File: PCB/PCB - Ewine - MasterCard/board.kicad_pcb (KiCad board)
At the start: 2 copper layers, 40.4 x 42 mm, 47 parts, among them J1 FH12-10S-0.5SH_55_, J10 DebugConnector, J2 527450697, J3 FH12-10S-0.5SH_55_, J4 1660, J5 Conn_02x04_Counter_Clockwise, J6 Conn_02x04_Counter_Clockwise, J7 Conn_02x04_Counter_Clockwise, J8 Conn_02x03_Counter_Clockwise, J9 Conn_02x04_Counter_Clockwise, SW1 reset_btn, U3 STM32WB55RGV7, Y1 CM8V-T1A-0.3-32.768KHZ-12.5PF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

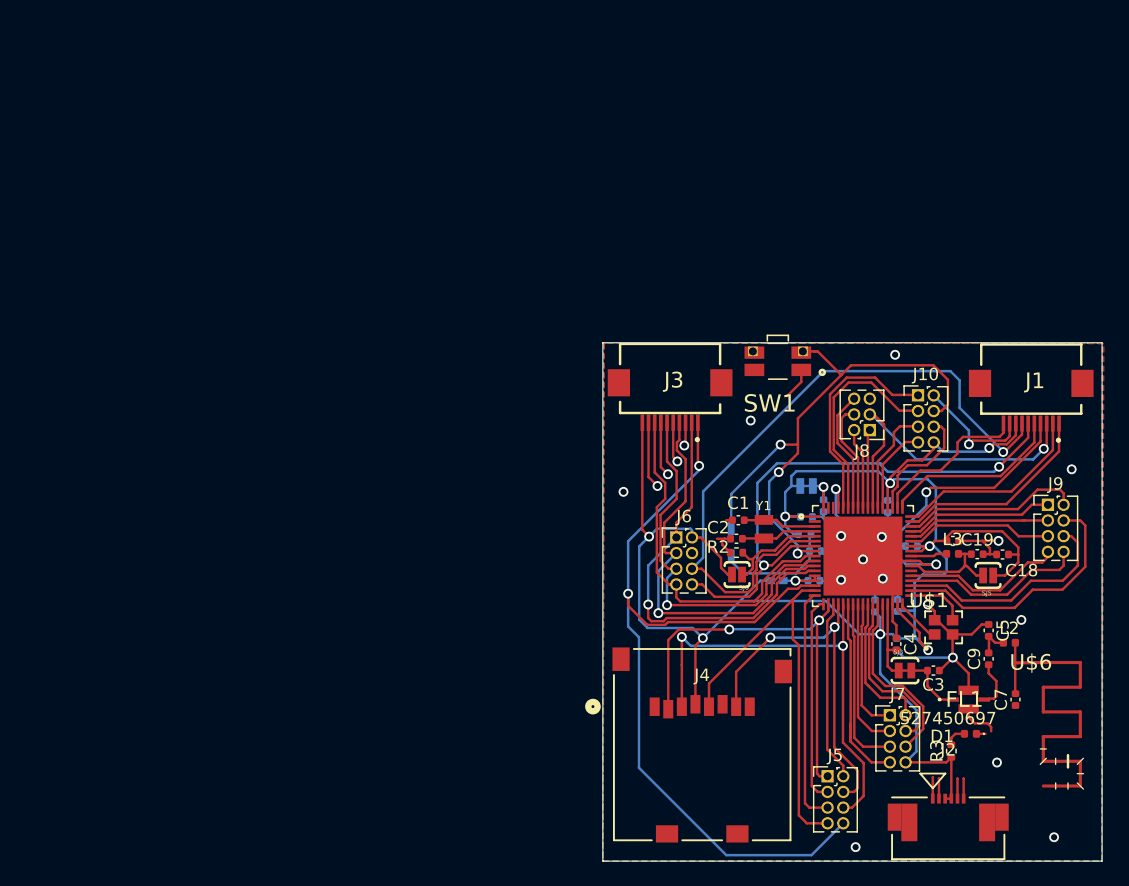
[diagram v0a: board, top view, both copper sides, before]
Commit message: pcb master card ok + il reste à mettre les pins des capteurs restants
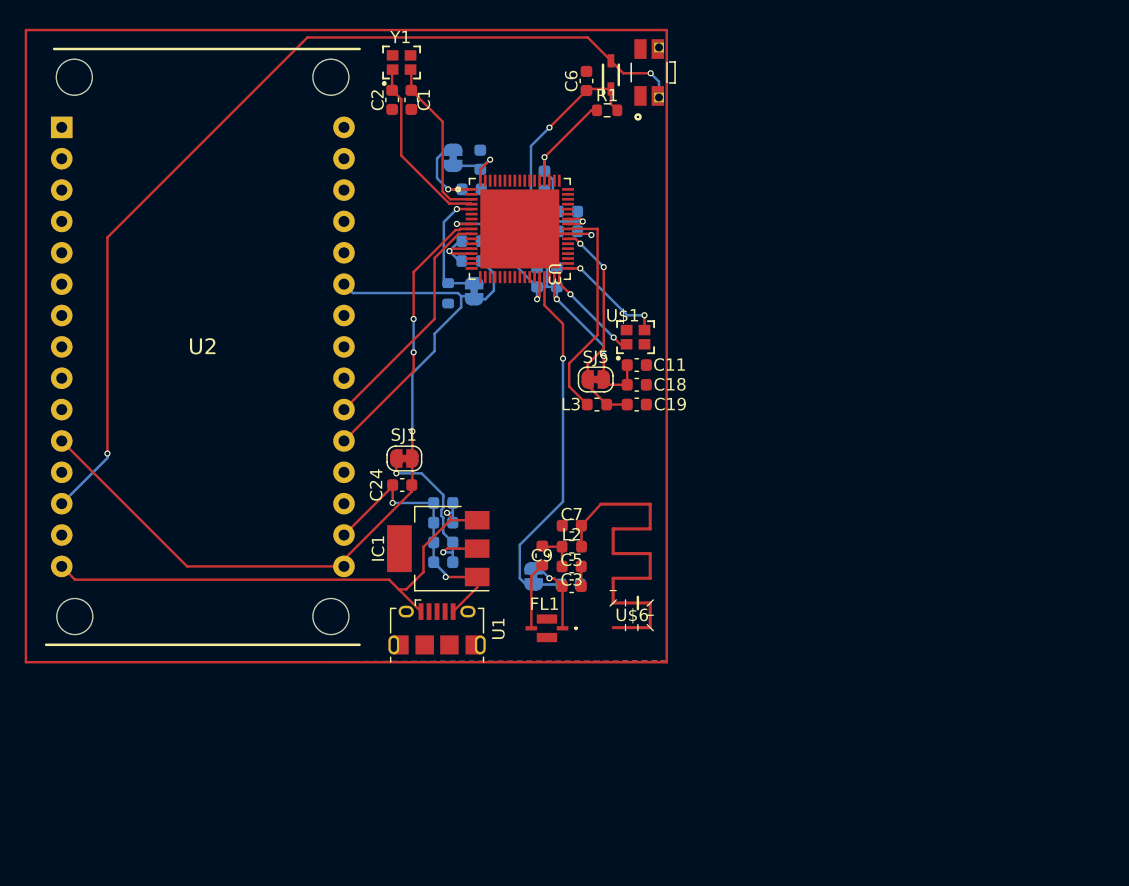
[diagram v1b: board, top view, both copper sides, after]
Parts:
- removed D1: LED, LED_SMD:LED_0402_1005Metric
- removed J1, J3: FH12-10S-0.5SH_55_, FH12-10S-0.5SH_55:FH12-10S-0.5SH(55)
- removed J10: DebugConnector, Connector_PinHeader_1.27mm:PinHeader_2x04_P1.27mm_Vertical
- removed J2: 527450697, ConnectorFPC0.5-6C:CON_527450697_MOL
- removed J4: 1660, CarteSD:CONN_1660_ADA
- removed J5, J6, J7, J9: Conn_02x04_Counter_Clockwise, Connector_PinHeader_1.27mm:PinHeader_2x04_P1.27mm_Vertical
- removed J8: Conn_02x03_Counter_Clockwise, Connector_PinHeader_1.27mm:PinHeader_2x03_P1.27mm_Vertical
- removed R3: 500, Resistor_SMD:R_0402_1005Metric
- added C20: 1µF, Capacitor_SMD:C_0603_1608Metric, B.Cu at (204.2, 74.0)
- added C21: 100nF, Capacitor_SMD:C_0603_1608Metric, B.Cu at (204.2, 75.6)
- added C22: 100nF, Capacitor_SMD:C_0603_1608Metric, B.Cu at (204.2, 77.2)
- added C23: 1µF, Capacitor_SMD:C_0603_1608Metric, B.Cu at (204.2, 78.8)
- added C24: 4.7µF, Capacitor_SMD:C_0603_1608Metric, F.Cu at (200.9, 72.5)
- added IC1: REG1117, Package_TO_SOT_SMD:SOT-223, F.Cu at (203.8, 77.7)
- added SJ1: JUMPER-PAD-2-NC_BY_TRACENO_SILK, Jumper:SolderJumper-2_P1.3mm_Bridged_RoundedPad1.0x1.5mm, F.Cu at (201.1, 70.4)
- added U1: 473460001, Connector_USB:USB_Micro-B_Amphenol_10118194_Horizontal, F.Cu at (203.7, 84.2)
- added U2: 113990105, footprint:113990105, F.Cu at (173.3, 43.6)
- C1, C10, C11, C12, C13, C14, C15, C16, C17, C18, C19, C2, C3, C5, C7, C8, C9: footprint Capacitor_SMD:C_0402_1005Metric -> Capacitor_SMD:C_0603_1608Metric
- C4: footprint Capacitor_SMD:C_0402_1005Metric -> Capacitor_SMD:C_0603_1608Metric; moved to B.Cu
- C6: footprint Capacitor_SMD:C_0402_1005Metric -> Capacitor_SMD:C_0603_1608Metric; moved to F.Cu
- D2: footprint BAT54:SOD2513X117N -> Library:STM32WB55RG_Diode; moved to F.Cu
- FL1: footprint PassBandFI212B245026-T:FI212B245026T -> Library:STM32WB55RG_PassBand
- L1: footprint board:IND_BLM15_0402_MUR -> Inductor_SMD:L_0603_1608Metric
- L2, L3: footprint Inductor_SMD:L_0402_1005Metric -> Inductor_SMD:L_0603_1608Metric
- R1: footprint Resistor_SMD:R_0402_1005Metric -> Resistor_SMD:R_0603_1608Metric; moved to F.Cu
- R2: footprint Resistor_SMD:R_0402_1005Metric -> Resistor_SMD:R_0603_1608Metric; moved to B.Cu
- SJ3: footprint board:PAD-JUMPER-2-NC_BY_TRACE_YES_SILK -> Jumper:SolderJumper-2_P1.3mm_Bridged_RoundedPad1.0x1.5mm; moved to B.Cu
- SJ4: footprint board:PAD-JUMPER-2-NC_BY_TRACE_NO_SILK -> Jumper:SolderJumper-2_P1.3mm_Bridged_RoundedPad1.0x1.5mm
- SJ5: footprint board:PAD-JUMPER-2-NC_BY_PASTE_YES_SILK -> Jumper:SolderJumper-2_P1.3mm_Bridged_RoundedPad1.0x1.5mm
- SJ6: footprint board:PAD-JUMPER-2-NC_BY_PASTE_YES_SILK -> Jumper:SolderJumper-2_P1.3mm_Bridged_RoundedPad1.0x1.5mm; moved to B.Cu
- SW1: footprint SideBtn434331013822:SW_434331013822 -> Library:STM32WB55RG_ResetButton
- U$1: footprint board:BT-XTAL_2016_N -> Library:STM32WB55RG_XTAL
- U$6: footprint board:QWMP_MEANDERED_LEFT_+6 -> Library:STM32WB55RG_BleAntenna
- U3: footprint STM32WB55RGV7:QFN40P800X800X100-69N -> Library:STM32WB55RG
- Y1: footprint board:XTAL_CM8V-T1A-0.3-32.768KHZ-12.5PF-100PPM-TC-QC -> Library:STM32WB55RG_XTAL
- moved Y1 49.5 mm to (199.8, 37.1), turned to 0 degrees
- moved C2 45.2 mm to (200.1, 41.4), turned to -90 degrees
- moved C14 44.0 mm to (214.3, 50.4), turned to 180 degrees
- moved C1 43.1 mm to (201.6, 41.4), turned to -90 degrees
- moved C6 42.4 mm to (215.8, 39.8), turned to -90 degrees
- moved C15 40.4 mm to (214.3, 52.0), turned to 180 degrees
- moved D2 40.3 mm to (213.8, 39.3)
- moved C13 39.5 mm to (207.2, 46.2), turned to 90 degrees
- moved SJ4 39.1 mm to (205.0, 46.0), turned to 90 degrees
- moved C17 39.1 mm to (206.5, 52.8)
- moved C7 38.6 mm to (214.6, 75.8), turned to 0 degrees
- moved C12 38.3 mm to (212.4, 47.9)
- moved C16 37.9 mm to (206.5, 48.6)
- moved R1 37.9 mm to (217.5, 42.2)
- moved U3 37.5 mm to (211.3, 52.2)
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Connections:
- U3 pad 10: ADC2 -> PC1
- U3 pad 11: ADC3 -> PC2
- U3 pad 12: ADC4 -> PC3
- U3 pad 15: ADC5 -> PA0
- U3 pad 16: CLK -> PA1
- U3 pad 19: CS -> PA4
- U3 pad 21: DO -> PA6
- U3 pad 22: DI -> PA7
- U3 pad 50: INT2 -> PC6
- U3 pad 51: INT1 -> PA10
- U3 pad 53: EN -> PA12
- U3 pad 58: GPIO -> PC10
- U3 pad 65: CS_D -> PB5
- U3 pad 9: ADC1 -> PC0
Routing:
- net ADC5: track 69.3 -> 0.00 mm, vias 2 -> 0
- net GND: track 87.4 -> 30.6 mm, vias 22 -> 3
- net PB8: track 55.5 -> 0.00 mm, vias 1 -> 0
- net PB9: track 45.3 -> 0.00 mm, vias 2 -> 0
- net 5V: track 0.00 -> 43.3 mm, vias 0 -> 1
- net VDD: track 165.6 -> 126.3 mm, vias 8 -> 7
- net DI: track 37.3 -> 0.00 mm, vias 2 -> 0
- net CLK: track 33.8 -> 0.00 mm
- net CS: track 33.5 -> 0.00 mm, vias 2 -> 0
- net ADC4: track 33.4 -> 0.00 mm, vias 1 -> 0
- net ADC3: track 32.8 -> 0.00 mm, vias 1 -> 0
- net NRST: track 45.6 -> 77.3 mm, vias 3 -> 2
- net ADC2: track 30.8 -> 0.00 mm, vias 1 -> 0
- net DO: track 29.4 -> 0.00 mm, vias 2 -> 0
- net ADC1: track 29.2 -> 0.00 mm
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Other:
- board outline removed

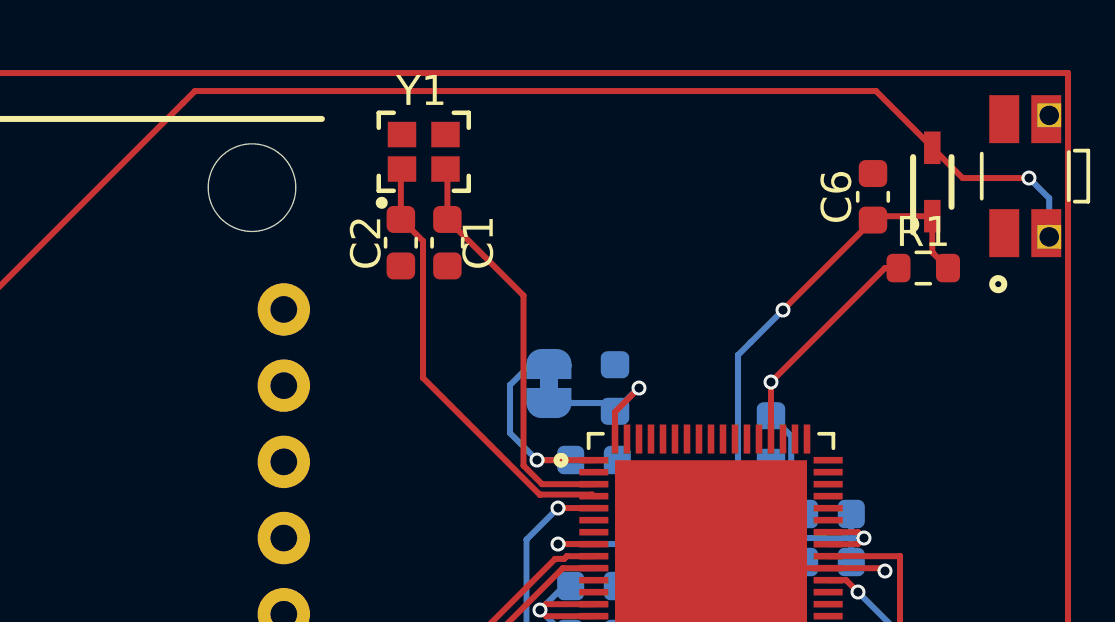
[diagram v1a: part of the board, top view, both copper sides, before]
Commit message: pcb master card add debug connector
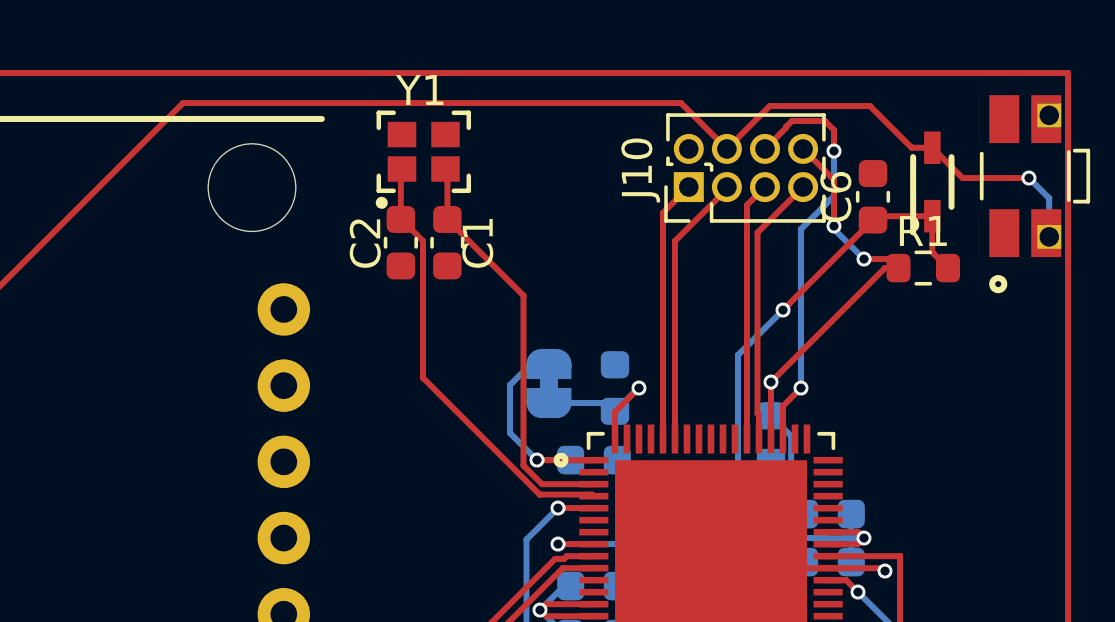
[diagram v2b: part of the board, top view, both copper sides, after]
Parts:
- added J10: DebugConnector, Connector_PinHeader_1.27mm:PinHeader_2x04_P1.27mm_Vertical, F.Cu at (209.7, 39.5)
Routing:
- net PA13_SWDIO: track 0.00 -> 13.8 mm, vias 0 -> 2
- net PB3_JTDO: track 0.00 -> 9.12 mm
- net PA14_SWCLOCK: track 0.00 -> 9.05 mm
- net PB4_NJTRST: track 0.00 -> 8.76 mm
- net PA15_JTDI: track 0.00 -> 8.65 mm
- net VDD: track 126.3 -> 132.1 mm, vias 7 -> 9
- net NRST: track 77.3 -> 78.1 mm
